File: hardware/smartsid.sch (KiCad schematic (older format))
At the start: 64 parts, among them P1 INPUT, P2 CONTROL, P3 POT2, P4 SOCKET LEFT, P5 OUTPUT, P6 SOCKET RIGHT, Q1 Q_NPN_BCE, Q2 Q_NPN_BCE, U1 GAL16V8, U2 SID2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

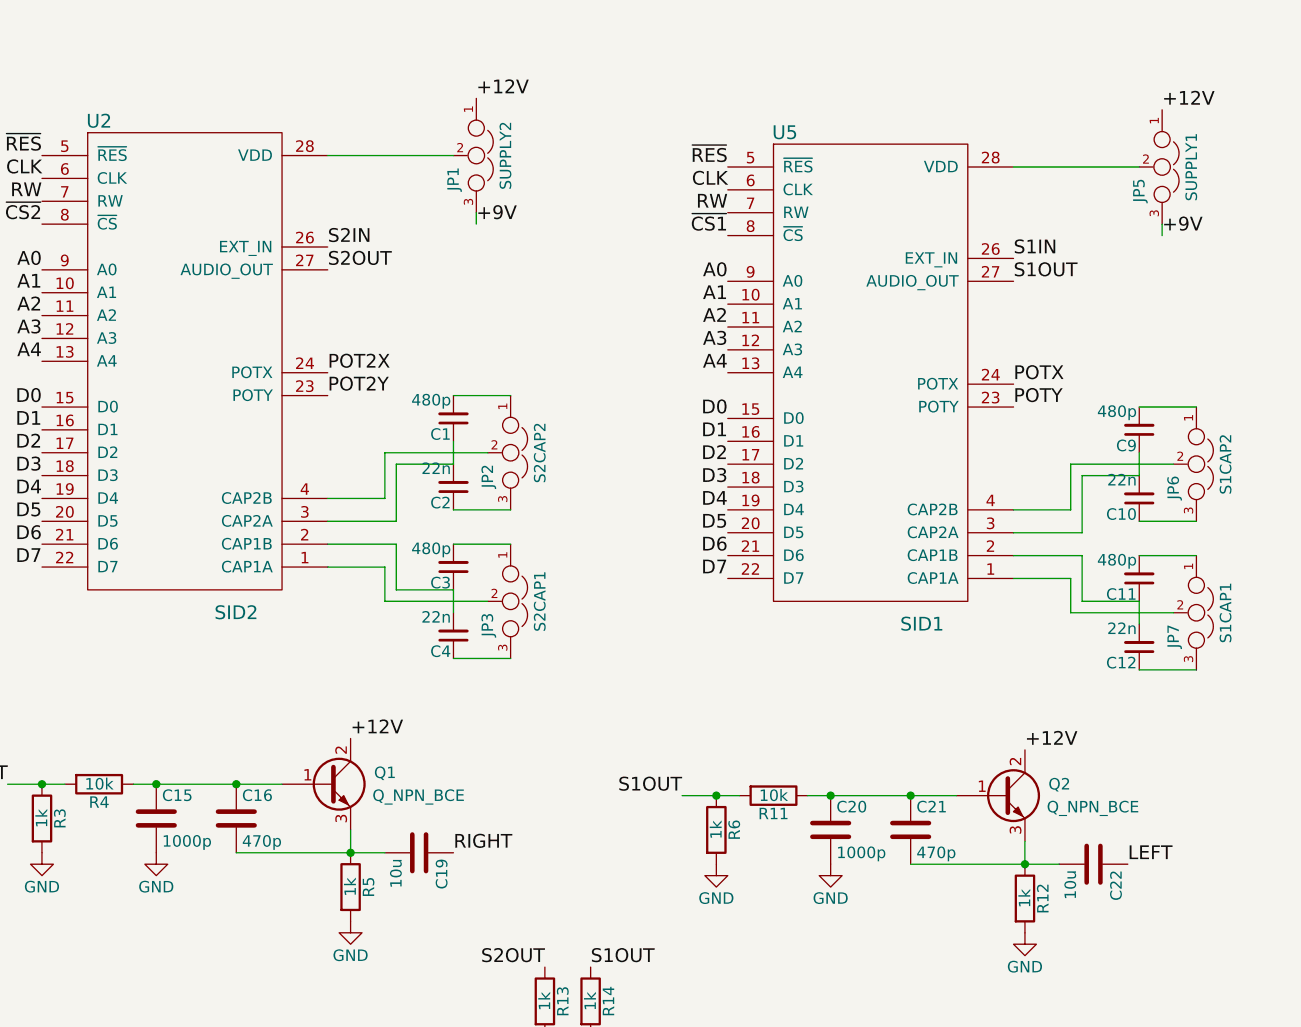
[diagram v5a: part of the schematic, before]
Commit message: Hardware: Fixed transistor symbols/footprints and extin jumper positions
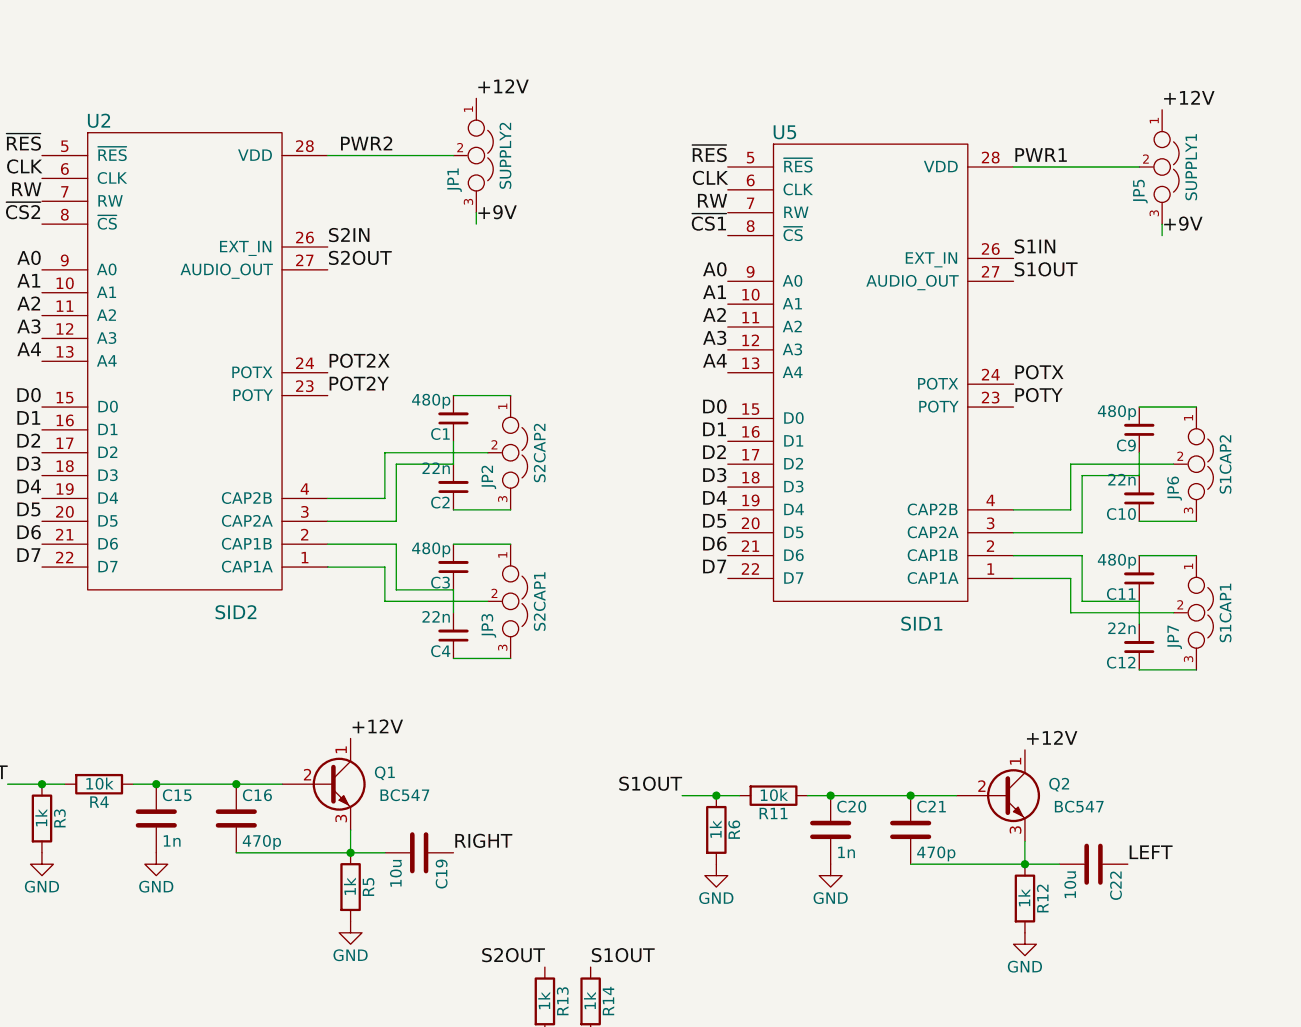
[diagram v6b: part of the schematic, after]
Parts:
- removed Q1, Q2: Q_NPN_BCE, TO_SOT_Packages_THT:TO-92_Inline_Narrow_Oval, symbol Q_NPN_BCE
- added Q1, Q2: BC547, TO_SOT_Packages_THT:TO-92_Inline_Narrow_Oval, symbol Q_NPN_CBE
- C15, C20: value 1000p -> 1n
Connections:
- net +12V: now also Q1.1 (C), Q2.1 (C)
- net PWR1: now reaches JP5.2, U5.28 (VDD)
- net PWR2: now reaches JP1.2, U2.28 (VDD)
- net at C15.1, C16.1, R4.1: now also Q1.2 (B)
- net at C16.2, C19.2, R5.1: now also Q1.3 (E)
- net at C20.1, C21.1, R11.1: now also Q2.2 (B)
- net at C21.2, C22.2, R12.1: now also Q2.3 (E)
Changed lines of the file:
@@
 P 2750 4250
 F 0 "C15" H 2775 4350 50  0000 L CNN
-F 1 "1000p" H 2775 4150 50  0000 L CNN
+F 1 "1n" H 2775 4150 50  0000 L CNN
 F 2 "Capacitors_ThroughHole:C_Disc_D3_P2.5" H 2788 4100 30  0001 C CNN
 F 3 "" H 2750 4250 60  0000 C CNN
@@
 Wire Wire Line
 	2650 4100 3300 4100
-$Comp
-L Q_NPN_BCE Q1
-U 1 1 56E6B555
-P 3500 4100
-F 0 "Q1" H 3800 4150 50  0000 R CNN
-F 1 "Q_NPN_BCE" H 4100 4050 50  0000 R CNN
-F 2 "TO_SOT_Packages_THT:TO-92_Inline_Narrow_Oval" H 3700 4200 29  0001 C CNN
-F 3 "" H 3500 4100 60  0000 C CNN
-	1    3500 4100
-	1    0    0    -1
-$EndComp
 Connection ~ 2750 4100
 $Comp
@@
 P 5700 4300
 F 0 "C20" H 5725 4400 50  0000 L CNN
-F 1 "1000p" H 5725 4200 50  0000 L CNN
+F 1 "1n" H 5725 4200 50  0000 L CNN
 F 2 "Capacitors_ThroughHole:C_Disc_D3_P2.5" H 5738 4150 30  0001 C CNN
 F 3 "" H 5700 4300 60  0000 C CNN
@@
 Wire Wire Line
 	5600 4150 6250 4150
-$Comp
-L Q_NPN_BCE Q2
-U 1 1 56E6CA42
-P 6450 4150
-F 0 "Q2" H 6750 4200 50  0000 R CNN
-F 1 "Q_NPN_BCE" H 7050 4100 50  0000 R CNN
-F 2 "TO_SOT_Packages_THT:TO-92_Inline_Narrow_Oval" H 6650 4250 29  0001 C CNN
-F 3 "" H 6450 4150 60  0000 C CNN
-	1    6450 4150
-	1    0    0    -1
-$EndComp
 Connection ~ 5700 4150
 $Comp
@@
 Text Label 1000 6900 2    60   ~ 0
 MONO_OUT
+$Comp
+L Q_NPN_CBE Q1
+U 1 1 56F03555
+P 3500 4100
+F 0 "Q1" H 3800 4150 50  0000 R CNN
+F 1 "BC547" H 3950 4050 50  0000 R CNN
+F 2 "TO_SOT_Packages_THT:TO-92_Inline_Narrow_Oval" H 3700 4200 29  0001 C CNN
+F 3 "" H 3500 4100 60  0000 C CNN
+	1    3500 4100
+	1    0    0    -1
+$EndComp
+$Comp
+L Q_NPN_CBE Q2
+U 1 1 56F0378B
+P 6450 4150
+F 0 "Q2" H 6750 4200 50  0000 R CNN
+F 1 "BC547" H 6900 4100 50  0000 R CNN
+F 2 "TO_SOT_Packages_THT:TO-92_Inline_Narrow_Oval" H 6650 4250 29  0001 C CNN
+F 3 "" H 6450 4150 60  0000 C CNN
+	1    6450 4150
+	1    0    0    -1
+$EndComp
+Text Label 3550 1350 0    60   ~ 0
+PWR2
+Text Label 6500 1400 0    60   ~ 0
+PWR1
 $EndSCHEMATC

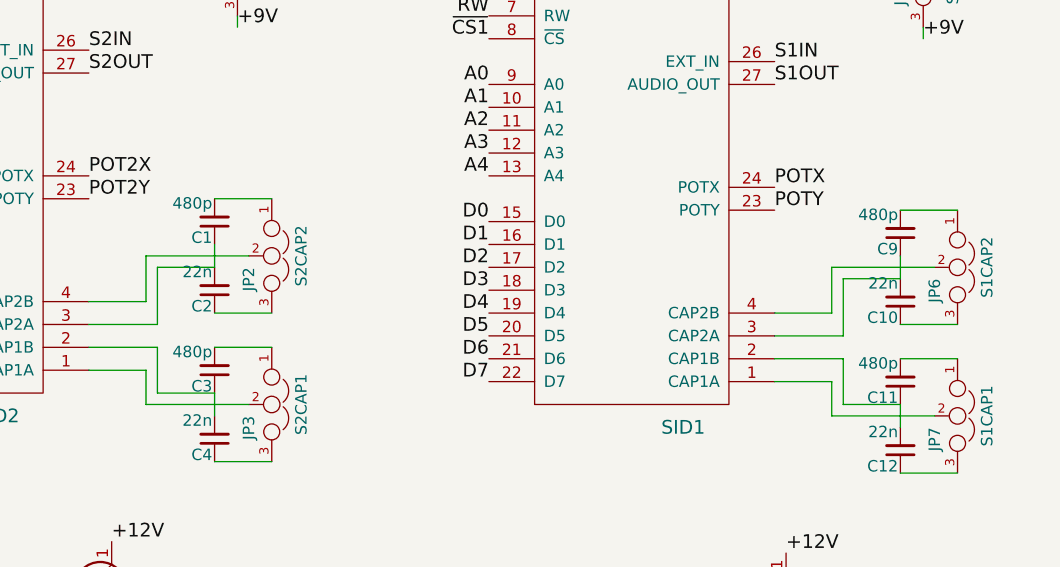
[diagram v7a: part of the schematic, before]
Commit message: Hardware: Corrected filter capacitor values for 6581 (470p)
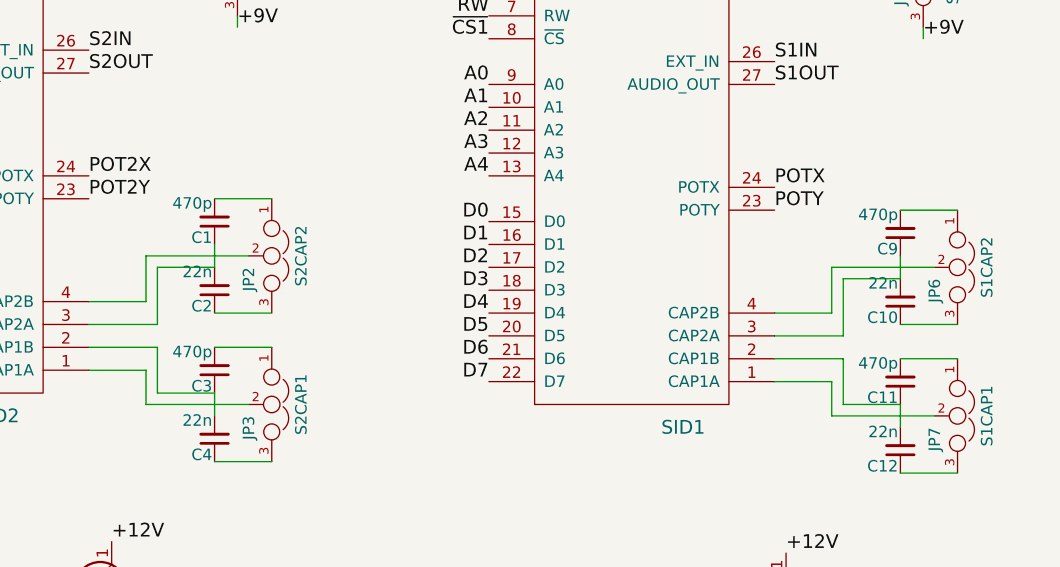
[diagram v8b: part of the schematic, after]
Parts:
- C1, C11, C3, C9: value 480p -> 470p
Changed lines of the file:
@@
 P 4050 2500
 F 0 "C1" H 4060 2570 50  0000 L CNN
-F 1 "480p" H 4060 2420 50  0000 L CNN
+F 1 "470p" H 4060 2420 50  0000 L CNN
 F 2 "Capacitors_ThroughHole:C_Disc_D3_P2.5" H 4050 2500 60  0001 C CNN
 F 3 "" H 4050 2500 60  0000 C CNN
@@
 P 4050 3150
 F 0 "C3" H 4060 3220 50  0000 L CNN
-F 1 "480p" H 4060 3070 50  0000 L CNN
+F 1 "470p" H 4060 3070 50  0000 L CNN
 F 2 "Capacitors_ThroughHole:C_Disc_D3_P2.5" H 4050 3150 60  0001 C CNN
 F 3 "" H 4050 3150 60  0000 C CNN
@@
 P 7050 2550
 F 0 "C9" H 7060 2620 50  0000 L CNN
-F 1 "480p" H 7060 2470 50  0000 L CNN
+F 1 "470p" H 7060 2470 50  0000 L CNN
 F 2 "Capacitors_ThroughHole:C_Disc_D3_P2.5" H 7050 2550 60  0001 C CNN
 F 3 "" H 7050 2550 60  0000 C CNN
@@
 P 7050 3200
 F 0 "C11" H 7060 3270 50  0000 L CNN
-F 1 "480p" H 7060 3120 50  0000 L CNN
+F 1 "470p" H 7060 3120 50  0000 L CNN
 F 2 "Capacitors_ThroughHole:C_Disc_D3_P2.5" H 7050 3200 60  0001 C CNN
 F 3 "" H 7050 3200 60  0000 C CNN
